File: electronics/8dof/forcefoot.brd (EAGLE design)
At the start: 120 x 32 mm, 112 parts

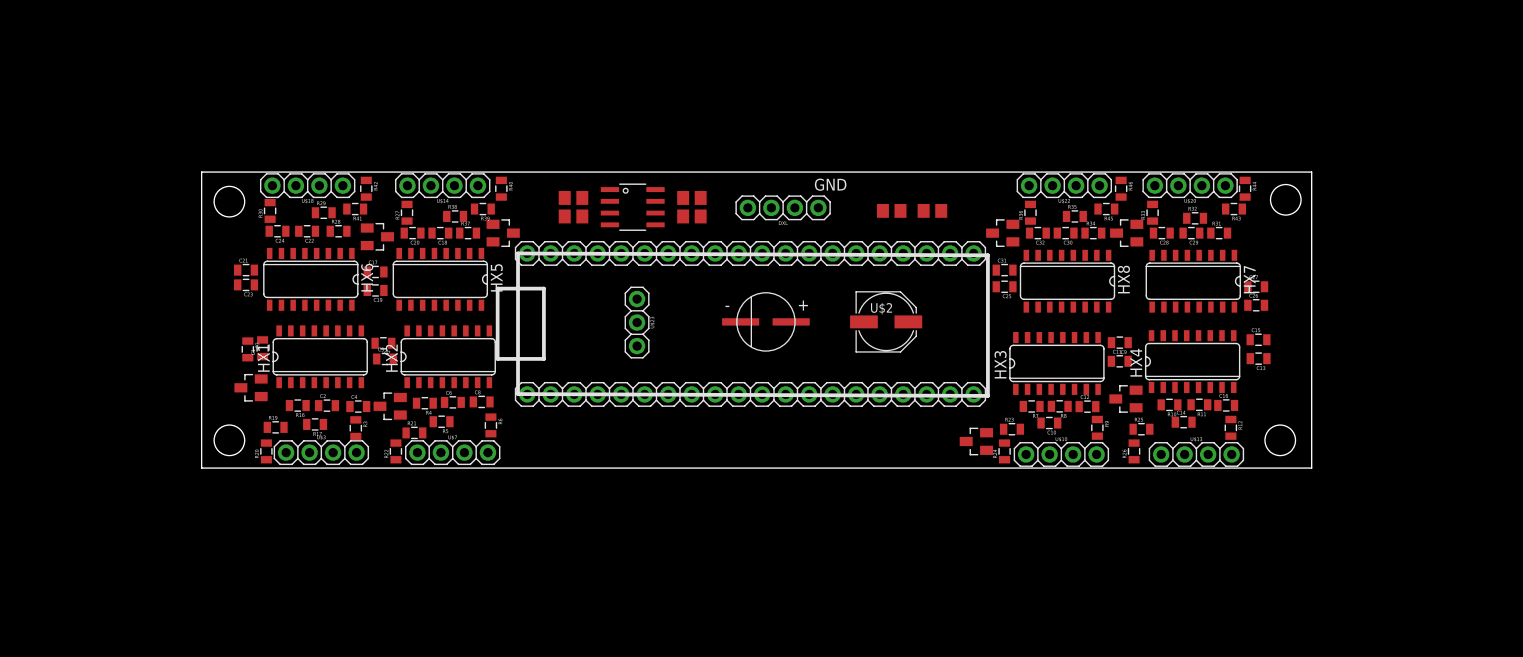
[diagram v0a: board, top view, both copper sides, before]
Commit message: Adding clock, tweaking placing
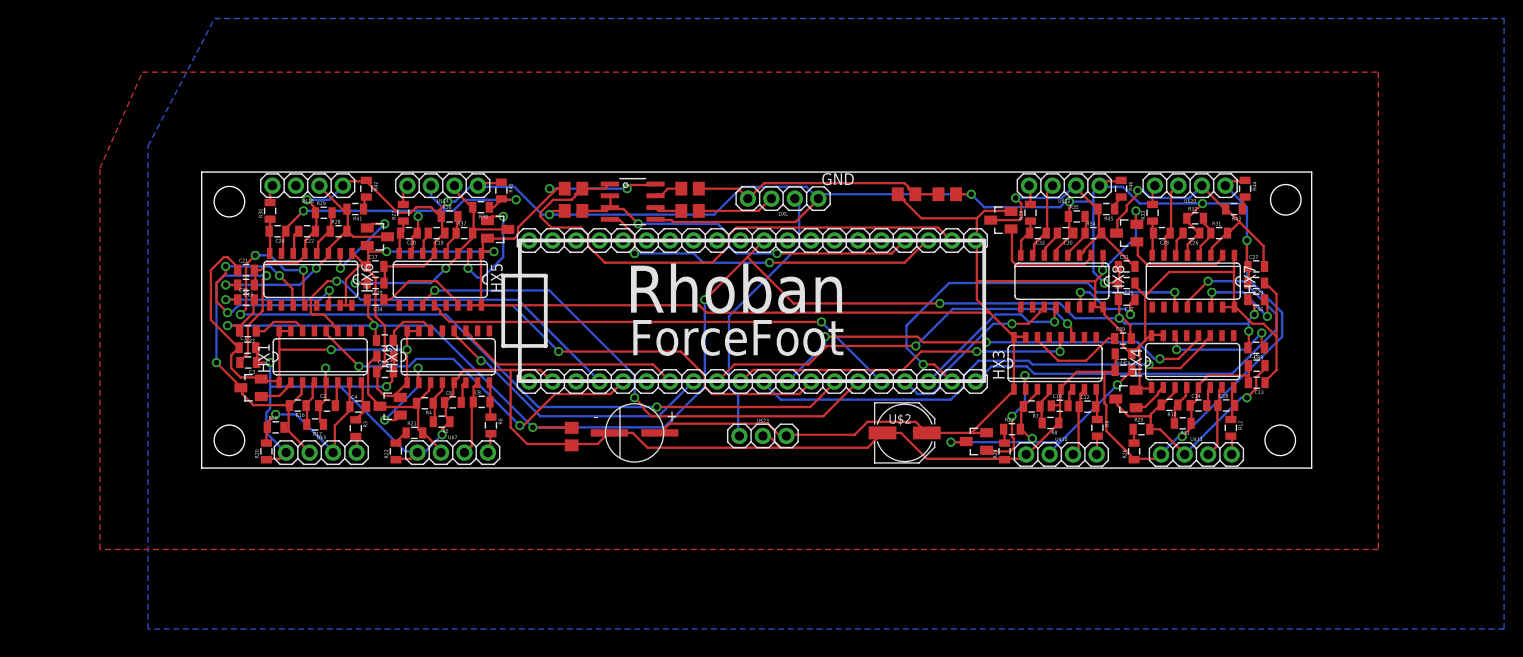
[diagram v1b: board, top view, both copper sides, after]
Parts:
- added C33, C34, C35, C36, C37, C38, C39, C40: 20pF, SparkFun-Passives:0805
- added R47: ?, rhoban:R0805
- moved U$23 20.1 mm to (59.4, 2.20), turned to 0 degrees
- moved U$4 18.6 mm to (46.8, 3.80)
- moved C25 13.2 mm to (100.0, 20.0)
- moved C31 13.2 mm to (100.0, 21.8)
- moved U$2 12.2 mm to (76.0, 3.80)
- moved C26 10.5 mm to (107.0, 25.4), turned to 180 degrees
- moved C29 8.84 mm to (114.0, 20.0)
- moved C15 2.81 mm to (114.0, 11.1)
- moved R11 2.69 mm to (106.1, 4.84)
- moved C13 2.61 mm to (114.1, 9.23)
- moved C14 2.41 mm to (107.8, 6.76)
- moved R2 2.41 mm to (76.2, 29.6)
- moved R18 2.41 mm to (80.6, 29.6)
- moved C27 2.20 mm to (114.0, 21.8)
- moved C10 2.17 mm to (92.8, 6.73), turned to 0 degrees
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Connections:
- net 5A+ renamed 6A+
- removed net 5A-: C20.1, HX5.7, R39.1, R40.2, U$14.3
- new net CLOCK: C33.2, C34.2, C35.2, C36.2, C37.2, C38.2, C39.2, C40.2, MAPLE_MINI.X8, R47.2
- new net N$16: C33.1, HX1.14
- new net N$17: C34.1, HX5.14
- new net N$18: C35.1, HX6.14
- new net N$19: C36.1, HX7.14
- new net N$20: C37.1, HX8.14
- new net N$21: C38.1, HX4.14
- new net N$22: C39.1, HX3.14
- new net N$23: C40.1, HX2.14
- net 5BASE: now also HX6.2, U$17.1; no longer HX5.2, U$11.1
- net 6A-: now also C20.1, HX5.7, R39.1, R40.2, U$14.3
- net 6BASE: now also HX5.2, U$11.1; no longer HX6.2, U$17.1
- net 7A-: now also C32.1, HX8.7, U$22.3; no longer C28.1, HX7.7, U$20.3
- net 7BASE: now also HX8.2, U$21.1; no longer HX7.2, U$19.1
- net 8A-: now also C28.1, HX7.7, U$20.3; no longer C32.1, HX8.7, U$22.3
- net 8BASE: now also HX7.2, U$19.1; no longer HX8.2, U$21.1
- net AVDD$5: now also C23.2, HX6.3, R28.2, R41.2, U$17.3, U$18.2; no longer C19.2, HX5.3, R37.2, R39.2, U$11.3, U$14.2
- net AVDD$6: now also C19.2, HX5.3, R37.2, R39.2, U$11.3, U$14.2; no longer C23.2, HX6.3, R28.2, R41.2, U$17.3, U$18.2
- net AVDD$7: now also C31.2, HX8.3, R34.2, R45.2, U$21.3, U$22.2; no longer C27.2, HX7.3, R31.2, R43.2, U$19.3, U$20.2
- net AVDD$8: now also C27.2, HX7.3, R31.2, R43.2, U$19.3, U$20.2; no longer C31.2, HX8.3, R34.2, R45.2, U$21.3, U$22.2
- net DOUT2: now also MAPLE_MINI.X19; no longer MAPLE_MINI.X18
- net DOUT3: now also MAPLE_MINI.X21; no longer MAPLE_MINI.X24
- net DOUT4: now also MAPLE_MINI.X23; no longer MAPLE_MINI.X26
- net DOUT5: now also HX6.12, MAPLE_MINI.X25; no longer HX5.12, MAPLE_MINI.X20
- net DOUT6: now also HX5.12, MAPLE_MINI.X27; no longer HX6.12, MAPLE_MINI.X22
- net DOUT7: now also HX8.12, MAPLE_MINI.X29; no longer HX7.12, MAPLE_MINI.X28
- net DOUT8: now also HX7.12, MAPLE_MINI.X31; no longer HX8.12, MAPLE_MINI.X30
- net GND: now also R47.1; no longer HX1.14, HX2.14, HX3.14, HX4.14, HX5.14, HX6.14, HX7.14, HX8.14
- net SCK2: now also MAPLE_MINI.X18; no longer MAPLE_MINI.X31
- net SCK3: now also MAPLE_MINI.X20; no longer MAPLE_MINI.X23
- net SCK4: now also MAPLE_MINI.X22; no longer MAPLE_MINI.X25
- net SCK5: now also HX6.11, MAPLE_MINI.X24; no longer HX5.11, MAPLE_MINI.X19
- net SCK6: now also HX5.11, MAPLE_MINI.X26; no longer HX6.11, MAPLE_MINI.X21
- net SCK7: now also HX8.11, MAPLE_MINI.X28; no longer HX7.11, MAPLE_MINI.X27
- net SCK8: now also HX7.11, MAPLE_MINI.X30; no longer HX8.11, MAPLE_MINI.X29
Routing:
- net GND: track 0.00 -> 433.1 mm, vias 0 -> 13
- net VCC: track 0.00 -> 352.4 mm, vias 0 -> 8
- net CLOCK: track 0.00 -> 159.7 mm, vias 0 -> 8
- net DOUT5: track 0.00 -> 86.5 mm, vias 0 -> 4
- net SCK5: track 0.00 -> 84.7 mm, vias 0 -> 4
- net RX: track 0.00 -> 59.5 mm
- net SCK6: track 0.00 -> 56.7 mm, vias 0 -> 2
- net SCK4: track 0.00 -> 53.5 mm, vias 0 -> 1
- net DOUT6: track 0.00 -> 51.9 mm, vias 0 -> 1
- net DOUT8: track 0.00 -> 49.8 mm, vias 0 -> 1
- net DOUT4: track 0.00 -> 49.1 mm, vias 0 -> 3
- net AVDD$1: track 0.00 -> 44.9 mm, vias 0 -> 2
- net SCK3: track 0.00 -> 43.5 mm, vias 0 -> 2
- net SCK1: track 0.00 -> 41.9 mm, vias 0 -> 1
- net SCK8: track 0.00 -> 41.8 mm, vias 0 -> 2
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- added copper zone on layer 1, net GND
- added copper zone on layer 16, net GND
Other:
- board text added: "ForceFoot"
- board text added: "Rhoban"

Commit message: Using 1.5mm 4p connectors
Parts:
- U$10, U$13, U$14, U$18, U$20, U$22, U$3, U$7: value CONNEC_1X04" -> CONNEC_1X041.5; device rhoban:CONNEC_1X04 -> rhoban:4P1.5
- moved U$13 1.71 mm to (104.4, 1.80)
- moved U$10 1.61 mm to (90.2, 1.80)
- moved U$20 1.52 mm to (108.8, 30.4)
- moved U$22 1.41 mm to (95.6, 30.4)
- moved U$14 1.26 mm to (28.2, 30.6)
- moved U$7 1.22 mm to (24.8, 1.60)
- moved U$18 1.22 mm to (14.2, 30.6)
- moved U$3 1.20 mm to (10.4, 1.60)
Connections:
- net 1A+: now also U$3.P$4; no longer U$3.4
- net 1A-: now also U$3.P$3; no longer U$3.3
- net 2A-: now also U$7.P$3; no longer U$7.3
- net 3A-: now also U$10.P$3; no longer U$10.3
- net 4A-: now also U$13.P$3; no longer U$13.3
- net 6A+: now also U$14.P$4; no longer U$14.4
- net 6A-: now also U$14.P$3; no longer U$14.3
- net 7A-: now also U$22.P$3; no longer U$22.3
- net 8A-: now also U$20.P$3; no longer U$20.3
- net AVDD$1: now also U$3.P$2; no longer U$3.2
- net AVDD$2: now also U$7.P$2; no longer U$7.2
- net AVDD$3: now also U$10.P$2; no longer U$10.2
- net AVDD$4: now also U$13.P$2; no longer U$13.2
- net AVDD$5: now also U$18.P$2; no longer U$18.2
- net AVDD$6: now also U$14.P$2; no longer U$14.2
- net AVDD$7: now also U$22.P$2; no longer U$22.2
- net AVDD$8: now also U$20.P$2; no longer U$20.2
- net GND: now also U$10.P$1, U$13.P$1, U$14.P$1, U$18.P$1, U$20.P$1, U$22.P$1, U$3.P$1, U$7.P$1; no longer U$10.1, U$13.1, U$14.1, U$18.1, U$20.1, U$22.1, U$3.1, U$7.1
- net N$10: now also U$18.P$4; no longer U$18.4
- net N$12: now also U$20.P$4; no longer U$20.4
- net N$14: now also U$22.P$4; no longer U$22.4
- net N$15: now also U$18.P$3; no longer U$18.3
- net N$4: now also U$7.P$4; no longer U$7.4
- net N$6: now also U$10.P$4; no longer U$10.4
- net N$8: now also U$13.P$4; no longer U$13.4
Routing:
- net CLOCK: track 159.7 -> 196.6 mm, vias 8 -> 10
- net GND: track 433.1 -> 465.8 mm, vias 13 -> 11
- net DOUT5: track 86.5 -> 63.7 mm, vias 4 -> 2
- net N$16: track 6.04 -> 28.4 mm, vias 0 -> 2
- net DOUT8: track 49.8 -> 28.5 mm
- net SCK5: track 84.7 -> 64.2 mm, vias 4 -> 2
- net RX: track 59.5 -> 43.4 mm
- net AVDD$1: track 44.9 -> 31.9 mm
- net VCC: track 352.4 -> 343.5 mm, vias 8 -> 6
- net AVDD$5: track 28.9 -> 37.4 mm, vias 2 -> 1
- net SCK8: track 41.8 -> 33.5 mm
- net 3BASE: track 13.1 -> 19.9 mm
- net 5BASE: track 10.5 -> 4.20 mm, vias 2 -> 0
- net SCK6: track 56.7 -> 50.7 mm, vias 2 -> 0
- net DOUT3: track 37.4 -> 43.2 mm, vias 2 -> 1
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
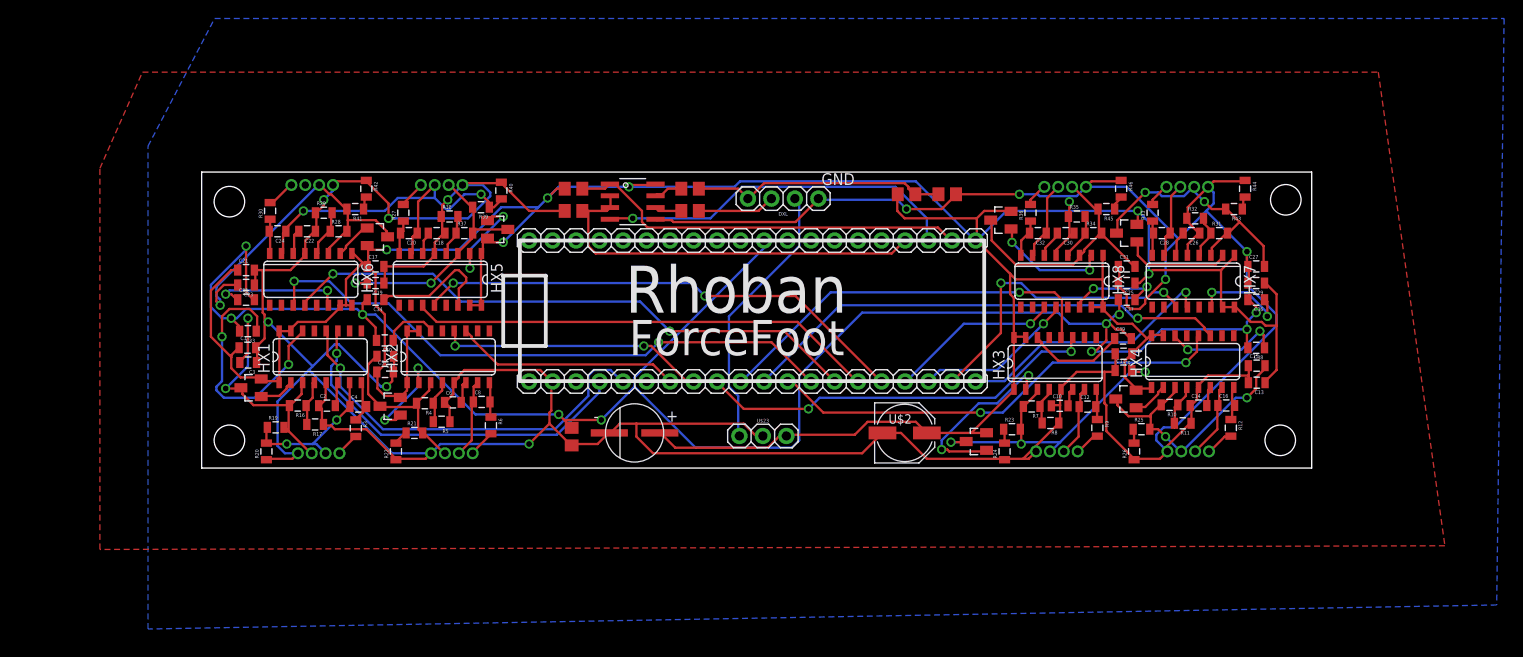
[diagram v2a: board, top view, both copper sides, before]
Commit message: Tying B-/B+ to ground
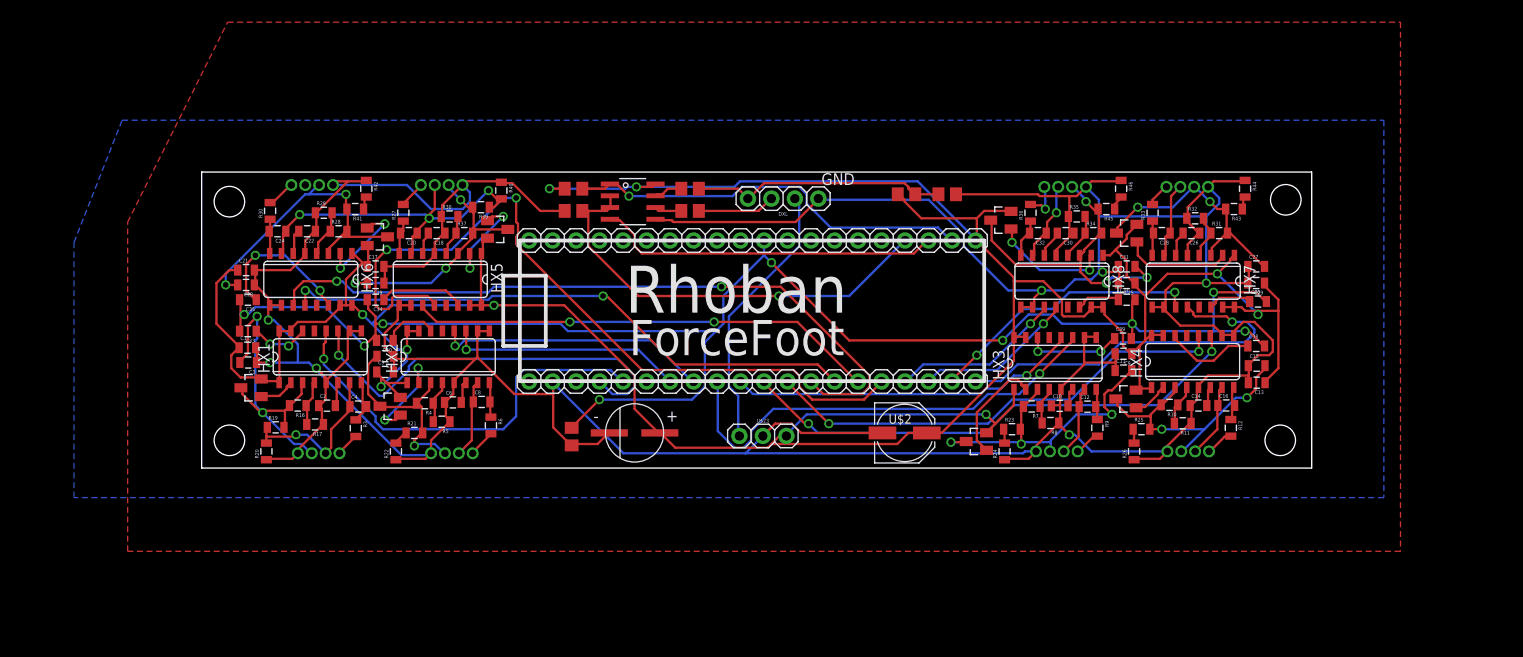
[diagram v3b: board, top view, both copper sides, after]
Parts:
- moved C36 0.28 mm to (114.2, 18.0), turned to 0 degrees
- moved C35 0.20 mm to (5.00, 18.2), turned to 180 degrees
- moved C38 0.20 mm to (114.0, 13.2), turned to 0 degrees
- turned C37 to 0 degrees
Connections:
- net GND: now also HX1.10, HX1.9, HX2.10, HX2.9, HX3.10, HX3.9, HX4.10, HX4.9, HX5.10, HX5.9, HX6.10, HX6.9, HX7.10, HX7.9, HX8.10, HX8.9
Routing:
- net DOUT6: track 54.0 -> 84.2 mm
- net GND: track 465.8 -> 495.2 mm, vias 11 -> 7
- net CLOCK: track 196.6 -> 172.8 mm, vias 10 -> 9
- net N$16: track 28.4 -> 6.52 mm
- net VCC: track 343.5 -> 361.5 mm, vias 6 -> 9
- net SCK5: track 64.2 -> 77.5 mm
- net DOUT8: track 28.5 -> 41.0 mm
- net 3BASE: track 19.9 -> 11.9 mm, vias 2 -> 0
- net SCK3: track 43.7 -> 50.2 mm, vias 2 -> 1
- net 5BASE: track 4.20 -> 10.5 mm, vias 0 -> 2
- net N$19: track 11.0 -> 4.89 mm, vias 2 -> 0
- net N$20: track 10.6 -> 4.81 mm, vias 2 -> 0
- net AVDD$7: track 30.0 -> 35.5 mm, vias 0 -> 3
- net DOUT3: track 43.2 -> 38.0 mm
- net N$17: track 14.0 -> 9.43 mm
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
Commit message: Update schema
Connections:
- removed net 1A-4: R41.1, R42.2
- removed net N$15: U$18.P$3
- new net 5A-: C24.1, HX6.7, R41.1, R42.2, U$18.P$3
- net 6A-: no longer C24.1, HX6.7
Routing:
- net VCC: track 361.5 -> 401.5 mm, vias 9 -> 8
- net CLOCK: track 172.8 -> 206.5 mm, vias 9 -> 7
- net DOUT6: track 84.2 -> 54.5 mm
- net 5A-: track 0.00 -> 20.0 mm, vias 0 -> 1
- net 6A-: track 39.5 -> 20.3 mm, vias 3 -> 1
- net GND: track 495.2 -> 476.0 mm, vias 7 -> 8
- net SCK5: track 77.5 -> 62.3 mm
- net DOUT5: track 63.3 -> 77.5 mm
- net SCK6: track 50.7 -> 63.0 mm
- net DOUT8: track 41.0 -> 29.4 mm, vias 1 -> 2
- net N$18: track 16.3 -> 23.4 mm
- net SCK1: track 45.0 -> 38.3 mm
- net AVDD$5: track 33.3 -> 29.4 mm, vias 2 -> 3
- net DIRECTION: track 47.3 -> 44.3 mm
- net DOUT1: track 45.0 -> 42.3 mm
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
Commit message: Fixes
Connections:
- removed net 1A-1: R21.1, R22.2
- removed net 1A-2: R23.1, R24.2
- removed net 1A-3: R25.1, R26.2
- removed net 1A-5: R43.1, R44.2
- removed net 1A-6: R45.1, R46.2
- net 2A-: now also R21.1, R22.2
- net 3A-: now also R23.1, R24.2
- net 4A-: now also R25.1, R26.2
- net 7A-: now also R45.1, R46.2
- net 8A-: now also R43.1, R44.2
- net DIRECTION: now also MAPLE_MINI.X3; no longer MAPLE_MINI.X2
- net DOUT4: now also MAPLE_MINI.X2; no longer MAPLE_MINI.X23
- net SCK5: now also MAPLE_MINI.X6; no longer MAPLE_MINI.X24
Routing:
- net VCC: track 401.5 -> 342.7 mm, vias 8 -> 11
- net AVDD$2: track 21.5 -> 65.0 mm, vias 1 -> 3
- net CLOCK: track 206.5 -> 172.1 mm
- net 4A-: track 8.15 -> 25.2 mm, vias 0 -> 2
- net DOUT5: track 77.5 -> 64.4 mm, vias 2 -> 3
- net DOUT4: track 51.1 -> 38.6 mm
- net N$18: track 23.4 -> 11.9 mm
- net AVDD$7: track 35.8 -> 46.6 mm, vias 3 -> 2
- net 8A-: track 8.35 -> 19.0 mm, vias 0 -> 2
- net 3A-: track 7.63 -> 18.1 mm, vias 0 -> 1
- net 2A-: track 8.48 -> 18.9 mm, vias 0 -> 1
- net TX: track 37.3 -> 46.2 mm, vias 0 -> 1
- net SCK3: track 50.2 -> 41.3 mm, vias 1 -> 2
- net 6A-: track 20.3 -> 28.9 mm
- net 7A-: track 8.77 -> 16.9 mm, vias 1 -> 2
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
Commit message: Fix
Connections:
- net DIRECTION: now also MAPLE_MINI.X2; no longer MAPLE_MINI.X3
- net DOUT4: now also MAPLE_MINI.X3; no longer MAPLE_MINI.X2
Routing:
- net GND: track 469.7 -> 0.00 mm, vias 12 -> 0
- net VCC: track 342.7 -> 0.00 mm, vias 11 -> 0
- net CLOCK: track 172.1 -> 0.00 mm, vias 7 -> 0
- net SCK5: track 67.0 -> 0.00 mm, vias 3 -> 0
- net AVDD$2: track 65.0 -> 0.00 mm, vias 3 -> 0
- net DOUT5: track 64.4 -> 0.00 mm, vias 3 -> 0
- net SCK6: track 56.4 -> 0.00 mm, vias 2 -> 0
- net SCK4: track 53.5 -> 0.00 mm, vias 2 -> 0
- net DOUT6: track 53.3 -> 0.00 mm, vias 3 -> 0
- net AVDD$7: track 46.6 -> 0.00 mm, vias 2 -> 0
- net TX: track 46.2 -> 0.00 mm, vias 1 -> 0
- net RX: track 44.3 -> 0.00 mm, vias 1 -> 0
- net SCK3: track 41.3 -> 0.00 mm, vias 2 -> 0
- net DIRECTION: track 40.9 -> 0.00 mm
- net DOUT1: track 40.8 -> 0.00 mm, vias 1 -> 0
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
